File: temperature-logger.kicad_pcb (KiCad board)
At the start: 4 copper layers, 106 x 50 mm, 157 parts, among them J1 USB, J10 DNP, J11 DNP, J2 THERMOCOUPLE, J3 THERMOCOUPLE, J4 THERMOCOUPLE, J5 THERMOCOUPLE, J6 OUT, J7 I2C, J8 DNP, J9 DNP, P1 TC2030, Q1 2N7002, Q2 BC817, Q3 2N7002, Q4 BC817, Q5 2N7002, Q6 BC817, SW1 SCPI_CSV, U1 USBLC6-4, U10 TLV9001, U11 TLV9001, U12 TLV9001, U13 USBLC6-4, U2 AP2204R-3.3, U3 STM32F072C8Tx, U4 MAX31855KASA, U5 MAX31855KASA, U6 MAX31855KASA, U7 MAX31855KASA, U8 DRV8837, U9 TLV9001

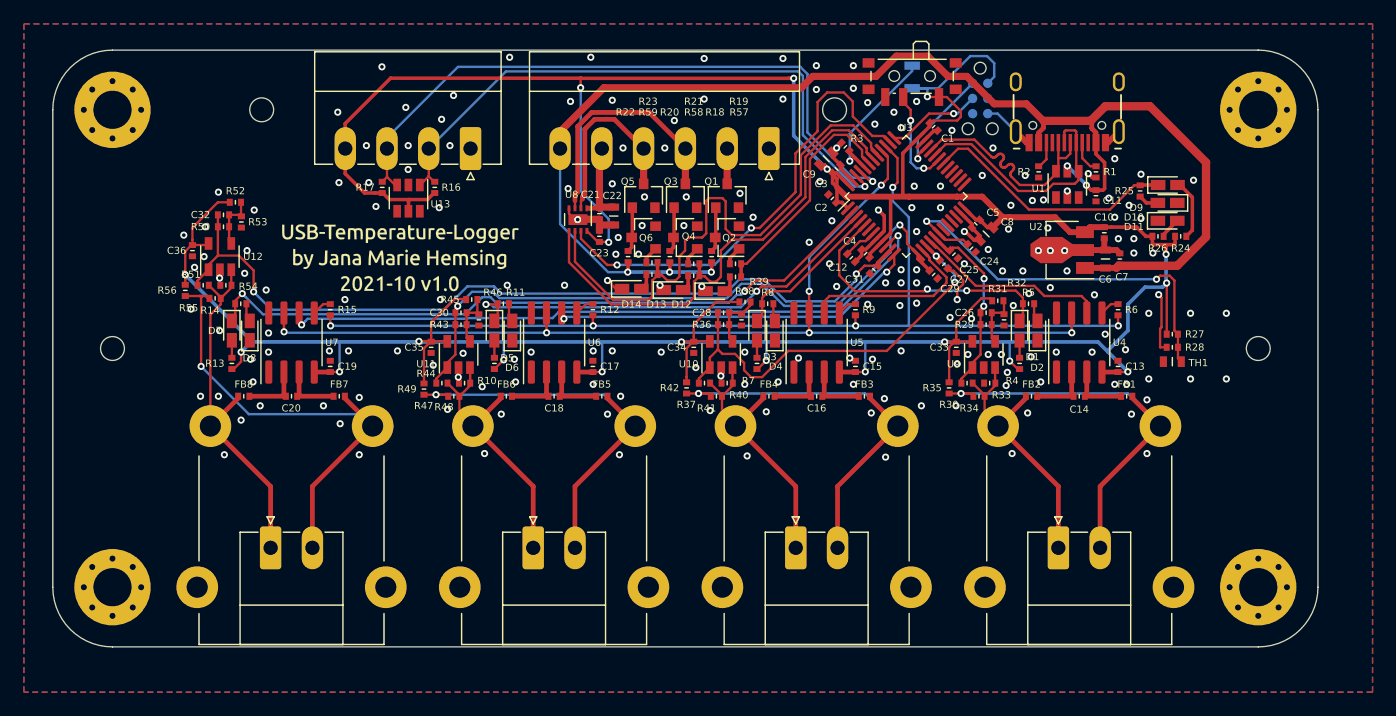
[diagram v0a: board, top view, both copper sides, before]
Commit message: Squeeze hardware to fit in 100mm width (JLC charges engineering fee for larger boards)
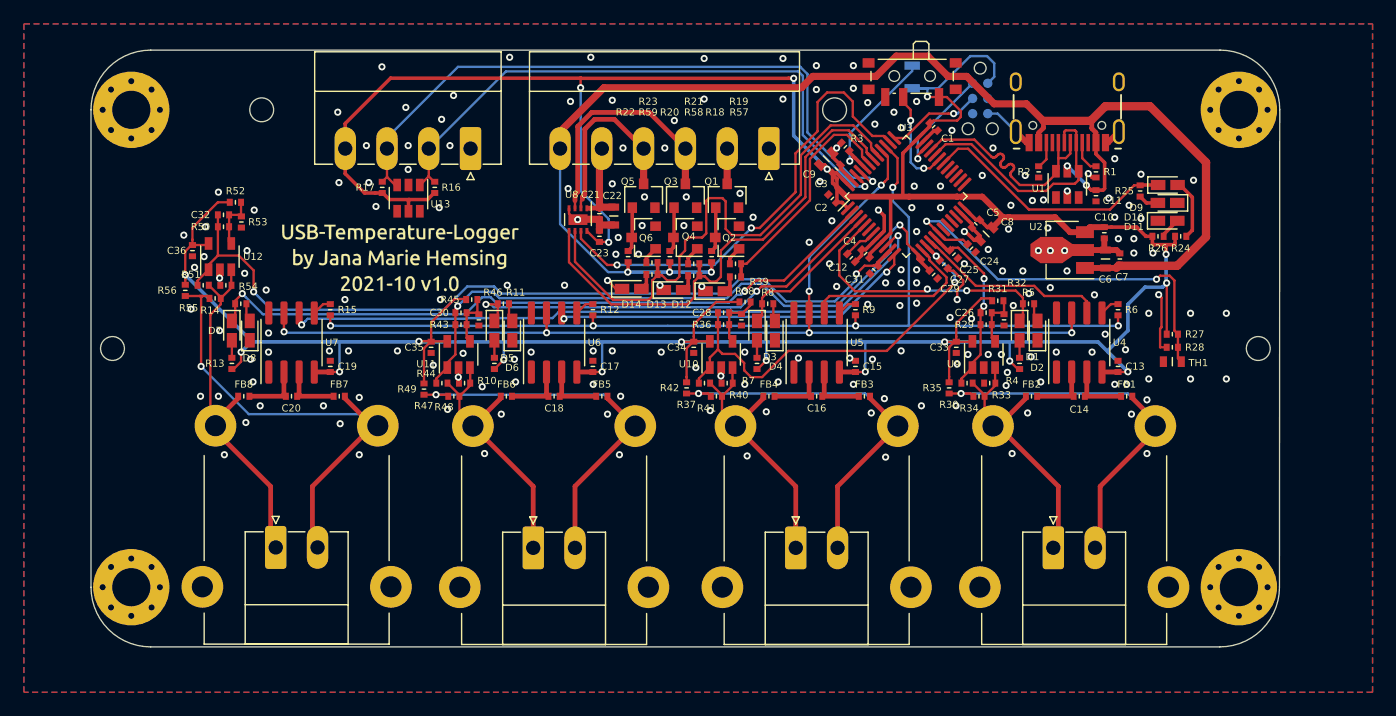
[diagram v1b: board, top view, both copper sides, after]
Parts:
- moved H2 1.62 mm to (149.4, 55.0)
- moved H4 1.62 mm to (149.4, 95.0)
- moved H1 1.58 mm to (56.6, 55.0)
- moved H3 1.58 mm to (56.6, 95.0)
- moved J11 0.43 mm to (70.4, 91.5)
- moved J5 0.43 mm to (70.4, 95.0)
- moved J2 0.43 mm to (135.6, 95.0)
- moved J8 0.43 mm to (135.6, 91.5)
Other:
- board size 106 x 50 mm -> 99.6 x 50 mm
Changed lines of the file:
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@@
   (net 100 "unconnected-(U13-Pad6)")
   (footprint "otter:PCC-SMP" (layer "F.Cu")
-    (at 136 95 180)
+    (at 135.575 94.995 180)
     (property "Sheetfile" "tsens.kicad_sch")
     (property "Sheetname" "Temperature_Sensor_0")
@@
   )
   (footprint "MountingHole:MountingHole_3.2mm_M3_Pad_Via" (layer "F.Cu")
-    (at 55 55)
+    (at 56.575 55)
     (descr "Mounting Hole 3.2mm, M3")
     (tags "mounting hole 3.2mm m3")
@@
   )
   (footprint "MountingHole:MountingHole_3.2mm_M3_Pad_Via" (layer "F.Cu")
-    (at 151 55)
+    (at 149.375 55)
     (descr "Mounting Hole 3.2mm, M3")
     (tags "mounting hole 3.2mm m3")
@@
   )
   (footprint "MountingHole:MountingHole_3.2mm_M3_Pad_Via" (layer "F.Cu")
-    (at 55 95)
+    (at 56.575 95)
     (descr "Mounting Hole 3.2mm, M3")
     (tags "mounting hole 3.2mm m3")
@@
   )
   (footprint "MountingHole:MountingHole_3.2mm_M3_Pad_Via" (layer "F.Cu")
-    (at 151 95)
+    (at 149.375 95)
     (descr "Mounting Hole 3.2mm, M3")
     (tags "mounting hole 3.2mm m3")
@@
   )
   (footprint "otter:PCC-SMP" (layer "F.Cu")
-    (at 70 95 180)
+    (at 70.43 94.9675 180)
     (property "Sheetfile" "tsens.kicad_sch")
     (property "Sheetname" "Temperature_Sensor_3")
@@
   )
   (footprint "otter:PhoenixContact_MC_1,5_2-G-3.5_1x02_P3.50mm_Horizontal" (layer "F.Cu")
-    (at 136 91.5)
+    (at 135.575 91.495)
     (descr "Generic Phoenix Contact connector footprint for: MC_1,5/2-G-3.5; number of pins: 02; pin pitch: 3.50mm; Angled || order number: 1844210 8A 160V")
     (tags "phoenix_contact connector MC_01x02_G_3.5mm")
@@
   )
   (footprint "otter:PhoenixContact_MC_1,5_2-G-3.5_1x02_P3.50mm_Horizontal" (layer "F.Cu")
-    (at 70 91.5)
+    (at 70.43 91.4675)
     (descr "Generic Phoenix Contact connector footprint for: MC_1,5/2-G-3.5; number of pins: 02; pin pitch: 3.50mm; Angled || order number: 1844210 8A 160V")
     (tags "phoenix_contact connector MC_01x02_G_3.5mm")
@@
   )
   (gr_line (start 120.575 50.9) (end 118.275 51.3) (layer "B.SilkS") (width 0.12))
-  (gr_arc (start 156 95) (mid 154.535534 98.535534) (end 151 100) (layer "Eco1.User") (width 0.15))
-  (gr_arc (start 151 50) (mid 154.535534 51.464466) (end 156 55) (layer "Eco1.User") (width 0.15))
-  (gr_line (start 156 55) (end 156 95) (layer "Eco1.User") (width 0.15))
-  (gr_arc (start 50 55) (mid 51.464466 51.464466) (end 55 50) (layer "Eco1.User") (width 0.15))
-  (gr_arc (start 55 100) (mid 51.464466 98.535534) (end 50 95) (layer "Eco1.User") (width 0.15))
-  (gr_line (start 50 95) (end 50 55) (layer "Eco1.User") (width 0.15))
-  (gr_line (start 55 50) (end 71.25 50) (layer "Eco1.User") (width 0.15))
+  (gr_arc (start 152.775 95) (mid 151.310534 98.535534) (end 147.775 100) (layer "Eco1.User") (width 0.15))
+  (gr_arc (start 147.8 50) (mid 151.335534 51.464466) (end 152.8 55) (layer "Eco1.User") (width 0.15))
+  (gr_line (start 152.8 55) (end 152.775 95) (layer "Eco1.User") (width 0.15))
+  (gr_arc (start 53.2 55) (mid 54.664466 51.464466) (end 58.2 50) (layer "Eco1.User") (width 0.15))
+  (gr_arc (start 58.2 100) (mid 54.664466 98.535534) (end 53.2 95) (layer "Eco1.User") (width 0.15))
+  (gr_line (start 53.2 95) (end 53.2 55) (layer "Eco1.User") (width 0.15))
+  (gr_line (start 58 50) (end 71.25 50) (layer "Eco1.User") (width 0.15))
   (gr_line (start 60 100) (end 60 60) (layer "Eco1.User") (width 0.15))
   (gr_line (start 71.25 50) (end 71.25 60) (layer "Eco1.User") (width 0.15))
-  (gr_line (start 151 50) (end 140.5 50) (layer "Eco1.User") (width 0.15))
+  (gr_line (start 147.8 50) (end 140.5 50) (layer "Eco1.User") (width 0.15))
   (gr_line (start 140.5 50) (end 129.575 50) (layer "Eco1.User") (width 0.15))
   (gr_line (start 140.5 60) (end 140.5 50) (layer "Eco1.User") (width 0.15))
-  (gr_line (start 151 100) (end 146 100) (layer "Eco1.User") (width 0.15))
+  (gr_line (start 148.6 100) (end 146 100) (layer "Eco1.User") (width 0.15))
   (gr_line (start 71.25 60) (end 60 60) (layer "Eco1.User") (width 0.15))
   (gr_line (start 117.375 50) (end 113.375 50) (layer "Eco1.User") (width 0.15))
   (gr_line (start 129.575 50) (end 117.375 50) (layer "Eco1.User") (width 0.15))
   (gr_line (start 146 60) (end 140.5 60) (layer "Eco1.User") (width 0.15))
-  (gr_line (start 55 100) (end 60 100) (layer "Eco1.User") (width 0.15))
+  (gr_line (start 57.8 100) (end 60 100) (layer "Eco1.User") (width 0.15))
   (gr_line (start 146 60) (end 146 100) (layer "Eco1.User") (width 0.15))
-  (gr_line (start 151 50) (end 55 50) (layer "Edge.Cuts") (width 0.05))
-  (gr_arc (start 50 55) (mid 51.464466 51.464466) (end 55 50) (layer "Edge.Cuts") (width 0.05))
-  (gr_arc (start 156 95) (mid 154.535534 98.535534) (end 151 100) (layer "Edge.Cuts") (width 0.05))
+  (gr_line (start 147.8 50) (end 58.2 50) (layer "Edge.Cuts") (width 0.05))
+  (gr_arc (start 53.2 55) (mid 54.664466 51.464466) (end 58.2 50) (layer "Edge.Cuts") (width 0.05))
+  (gr_arc (start 152.775 95) (mid 151.310534 98.535534) (end 147.775 100) (layer "Edge.Cuts") (width 0.05))
   (gr_circle (center 115.5 55) (end 116.5 55) (layer "Edge.Cuts") (width 0.05) (fill none))
-  (gr_arc (start 151 50) (mid 154.535534 51.464466) (end 156 55) (layer "Edge.Cuts") (width 0.05))
+  (gr_arc (start 147.8 50) (mid 151.335534 51.464466) (end 152.8 55) (layer "Edge.Cuts") (width 0.05))
   (gr_circle (center 67.5 55) (end 68.5 55) (layer "Edge.Cuts") (width 0.05) (fill none))
-  (gr_line (start 156 95) (end 156 55) (layer "Edge.Cuts") (width 0.05))
-  (gr_line (start 55 100) (end 151 100) (layer "Edge.Cuts") (width 0.05))
-  (gr_line (start 50 55) (end 50 95) (layer "Edge.Cuts") (width 0.05))
-  (gr_arc (start 55 100) (mid 51.464466 98.535534) (end 50 95) (layer "Edge.Cuts") (width 0.05))
+  (gr_line (start 152.775 95) (end 152.8 55) (layer "Edge.Cuts") (width 0.05))
+  (gr_line (start 58.2 100) (end 147.775 100) (layer "Edge.Cuts") (width 0.05))
+  (gr_line (start 53.2 55) (end 53.2 95) (layer "Edge.Cuts") (width 0.05))
+  (gr_arc (start 58.2 100) (mid 54.664466 98.535534) (end 53.2 95) (layer "Edge.Cuts") (width 0.05))
   (gr_circle (center 55 75) (end 56 75) (layer "Edge.Cuts") (width 0.05) (fill none))
   (gr_circle (center 151 75) (end 152 75) (layer "Edge.Cuts") (width 0.05) (fill none))
@@
   (via (at 96.875 54.2) (size 0.6) (drill 0.3) (layers "F.Cu" "B.Cu") (net 2))
   (via (at 129.875 78.1) (size 0.6) (drill 0.3) (layers "F.Cu" "B.Cu") (net 2))
-  (via (at 65.775 81) (size 0.6) (drill 0.3) (layers "F.Cu" "B.Cu") (net 2))
+  (via (at 66.175 81.2) (size 0.6) (drill 0.3) (layers "F.Cu" "B.Cu") (net 2))
   (via (at 96.475 80.5) (size 0.6) (drill 0.3) (layers "F.Cu" "B.Cu") (net 2))
   (via (at 77.075 63.1) (size 0.6) (drill 0.3) (layers "F.Cu" "B.Cu") (net 2))
@@
       (pts
         (xy 58.675 79.75)
-        (xy 59.675 80.75)
-        (xy 59.675 100.25)
-        (xy 58.675 100.25)
-        (xy 58.675 81.25)
+        (xy 60.675 80.75)
+        (xy 60.675 100.25)
+        (xy 59.275 100.25)
+        (xy 59.275 81.25)
         (xy 57.675 80.25)
         (xy 57.675 71.75)
@@
       (pts
         (xy 146.175 79.8)
-        (xy 147.175 80.8)
-        (xy 147.175 100.3)
-        (xy 146.175 100.3)
-        (xy 146.175 81.3)
+        (xy 146.575 80.8)
+        (xy 146.575 100.3)
+        (xy 145.375 100.3)
+        (xy 145.375 81.3)
         (xy 145.175 80.3)
         (xy 145.175 78.4)
